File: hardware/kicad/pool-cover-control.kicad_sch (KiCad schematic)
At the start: 70 parts, among them J1 Power_Supply _Conn, J2 Motor_Conn, J3 Key_Switch_Conn, J4 Limit_Switch_Conn, J5 SWD_Conn, Q1 DMP4015SK3Q-13, U1 STM32G031K8Tx, U2 ULN2003A, U3 LMR14206, U4 PC817, U5 PC817, U6 PC817, U7 PC817

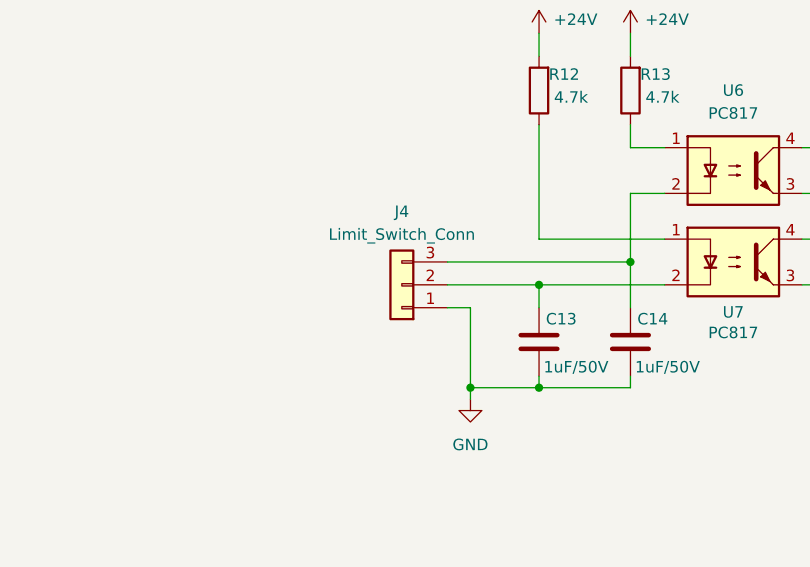
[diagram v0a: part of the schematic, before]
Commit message: feat(hardware): add 24 vcc pin to limit switch conn for flexibility
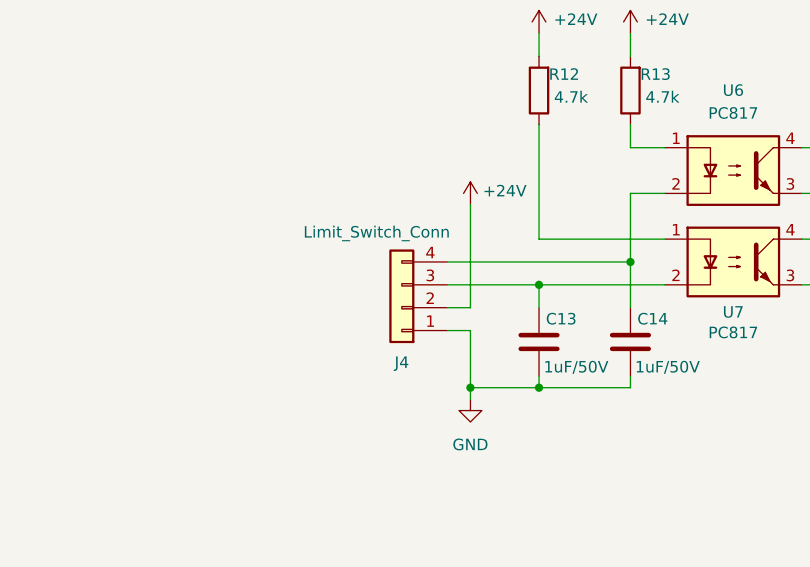
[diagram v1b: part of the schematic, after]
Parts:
- removed J4: Limit_Switch_Conn, TerminalBlock_Phoenix:TerminalBlock_Phoenix_MKDS-1,5-3-5.08_1x03_P5.08mm_Horizontal, symbol Connector_Generic:Conn_01x03
- added J4: Limit_Switch_Conn, TerminalBlock_Phoenix:TerminalBlock_Phoenix_MKDS-1,5-4-5.08_1x04_P5.08mm_Horizontal, symbol Connector_Generic:Conn_01x04
- C13, C14, C15, C16: footprint Capacitor_SMD:C_0402_1005Metric -> Capacitor_SMD:C_0603_1608Metric
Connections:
- net +24V: now also J4.2 (Pin_2)
- net GND: now also J4.1 (Pin_1)
- net at C14.2, U6.2: now also J4.4 (Pin_4)
- net at C13.2, U7.2: now also J4.3 (Pin_3)
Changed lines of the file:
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@@
 	)
 	(junction
-		(at 251.46 143.51)
-		(diameter 0)
-		(color 0 0 0 0)
-	)
-	(junction
 		(at 102.87 134.62)
 		(diameter 0)
@@
 	)
 	(junction
+		(at 251.46 143.51)
+		(diameter 0)
+		(color 0 0 0 0)
+	)
+	(junction
 		(at 259.08 132.08)
 		(diameter 0)
@@
 	(wire
 		(pts
+			(xy 251.46 137.16) (xy 251.46 143.51)
+		)
+		(stroke
+			(width 0)
+			(type default)
+		)
+	)
+	(wire
+		(pts
 			(xy 113.03 114.3) (xy 106.68 114.3)
 		)
@@
 	(wire
 		(pts
+			(xy 248.92 137.16) (xy 251.46 137.16)
+		)
+		(stroke
+			(width 0)
+			(type default)
+		)
+	)
+	(wire
+		(pts
 			(xy 125.73 189.23) (xy 142.24 189.23)
 		)
@@
 	(wire
 		(pts
-			(xy 251.46 134.62) (xy 248.92 134.62)
-		)
-		(stroke
-			(width 0)
-			(type default)
-		)
-	)
-	(wire
-		(pts
 			(xy 175.26 134.62) (xy 181.61 134.62)
 		)
@@
 	(wire
 		(pts
-			(xy 251.46 134.62) (xy 251.46 143.51)
-		)
-		(stroke
-			(width 0)
-			(type default)
-		)
-	)
-	(wire
-		(pts
 			(xy 248.92 132.08) (xy 259.08 132.08)
 		)
@@
 		)
 	)
+	(wire
+		(pts
+			(xy 248.92 134.62) (xy 251.46 134.62)
+		)
+		(stroke
+			(width 0)
+			(type default)
+		)
+	)
+	(wire
+		(pts
+			(xy 251.46 134.62) (xy 251.46 123.19)
+		)
+		(stroke
+			(width 0)
+			(type default)
+		)
+	)
 	(text "Reverse Polarity Protection\nP-channel MOSFET in series with the supply rail, gate clamped to −18V by a Zener diode,\nthat blocks current silently if the PSU is connected with reversed polarity."
 		(exclude_from_sim no)
@@
 			)
 		)
-		(property "Footprint" "Capacitor_SMD:C_0402_1005Metric"
+		(property "Footprint" "Capacitor_SMD:C_0603_1608Metric"
 			(at 258.1148 134.62 0)
 			(effects
@@
 			)
 		)
-		(property "Footprint" "Capacitor_SMD:C_0402_1005Metric"
+		(property "Footprint" "Capacitor_SMD:C_0603_1608Metric"
 			(at 268.2748 134.62 0)
 			(effects
@@
 			)
 		)
-		(property "Footprint" "Capacitor_SMD:C_0402_1005Metric"
+		(property "Footprint" "Capacitor_SMD:C_0603_1608Metric"
 			(at 258.1148 76.2 0)
 			(effects
@@
 	)
 	(symbol
+		(lib_id "power:+24V")
+		(at 251.46 123.19 0)
+		(unit 1)
+		(exclude_from_sim no)
+		(in_bom yes)
+		(on_board yes)
+		(dnp no)
+		(property "Reference" "#PWR1"
+			(at 251.46 127 0)
+			(effects
+				(font
+					(size 1.27 1.27)
+				)
+				(hide yes)
+			)
+		)
+		(property "Value" "+24V"
+			(at 255.27 121.666 0)
+			(effects
+				(font
+					(size 1.27 1.27)
+				)
+			)
+		)
+		(property "Footprint" ""
+			(at 251.46 123.19 0)
+			(effects
+				(font
+					(size 1.27 1.27)
+				)
+				(hide yes)
+			)
+		)
+		(property "Datasheet" ""
+			(at 251.46 123.19 0)
+			(effects
+				(font
+					(size 1.27 1.27)
+				)
+				(hide yes)
+			)
+		)
+		(property "Description" "Power symbol creates a global label with name \"+24V\""
+			(at 251.46 123.19 0)
+			(effects
+				(font
+					(size 1.27 1.27)
+				)
+				(hide yes)
+			)
+		)
+		(pin "1"
+		)
+		(instances
+			(project "pool-cover-control"
+				(path "/5c20c9eb-2c9b-4810-9f42-05cc49ca5670"
+					(reference "#PWR1")
+					(unit 1)
+				)
+			)
+		)
+	)
+	(symbol
 		(lib_id "Device:C")
 		(at 163.83 189.23 270)
@@
 	)
 	(symbol
-		(lib_id "Connector_Generic:Conn_01x03")
-		(at 243.84 132.08 180)
-		(unit 1)
-		(exclude_from_sim no)
-		(in_bom yes)
-		(on_board yes)
-		(dnp no)
-		(property "Reference" "J4"
-			(at 243.84 123.952 0)
-			(effects
-				(font
-					(size 1.27 1.27)
-				)
-			)
-		)
-		(property "Value" "Limit_Switch_Conn"
-			(at 243.84 126.492 0)
-			(effects
-				(font
-					(size 1.27 1.27)
-				)
-			)
-		)
-		(property "Footprint" "TerminalBlock_Phoenix:TerminalBlock_Phoenix_MKDS-1,5-3-5.08_1x03_P5.08mm_Horizontal"
-			(at 243.84 132.08 0)
-			(effects
-				(font
-					(size 1.27 1.27)
-				)
-				(hide yes)
-			)
-		)
-		(property "Datasheet" "~"
-			(at 243.84 132.08 0)
-			(effects
-				(font
-					(size 1.27 1.27)
-				)
-				(hide yes)
-			)
-		)
-		(property "Description" "Generic connector, single row, 01x03, script generated (kicad-library-utils/schlib/autogen/connector/)"
-			(at 243.84 132.08 0)
-			(effects
-				(font
-					(size 1.27 1.27)
-				)
-				(hide yes)
-			)
-		)
-		(property "LCSC" "C91154"
-			(at 243.84 132.08 0)
-			(effects
-				(font
-					(size 1.27 1.27)
-				)
-				(hide yes)
-			)
-		)
-		(pin "1"
-		)
-		(pin "2"
-		)
-		(pin "3"
-		)
-		(instances
-			(project "pool-cover-control"
-				(path "/5c20c9eb-2c9b-4810-9f42-05cc49ca5670"
-					(reference "J4")
-					(unit 1)
-				)
-			)
-		)
-	)
-	(symbol
 		(lib_id "Device:R")
 		(at 171.45 189.23 270)
@@
 			)
 		)
-		(property "Footprint" "Capacitor_SMD:C_0402_1005Metric"
+		(property "Footprint" "Capacitor_SMD:C_0603_1608Metric"
 			(at 268.2748 76.2 0)
 			(effects
@@
 					(unit 1)
 				)
+			)
+		)
+	)
+	(symbol
+		(lib_id "Connector_Generic:Conn_01x04")
+		(at 243.84 134.62 180)
+		(unit 1)
+		(exclude_from_sim no)
+		(in_bom yes)
+		(on_board yes)
+		(dnp no)
+		(property "Reference" "J4"
+			(at 243.84 140.716 0)
+			(effects
+				(font
+					(size 1.27 1.27)
+				)
+			)
+		)
+		(property "Value" "Limit_Switch_Conn"
+			(at 241.046 126.238 0)
+			(effects
+				(font
+					(size 1.27 1.27)
+				)
+			)
+		)
+		(property "Footprint" "TerminalBlock_Phoenix:TerminalBlock_Phoenix_MKDS-1,5-4-5.08_1x04_P5.08mm_Horizontal"
+			(at 243.84 134.62 0)
+			(effects
+				(font
+					(size 1.27 1.27)
+				)
+				(hide yes)
+			)
+		)
+		(property "Datasheet" "docs/datasheets/PhoenixContact1712805.pdf"
+			(at 243.84 134.62 0)
+			(effects
+				(font
+					(size 1.27 1.27)
+				)
+				(hide yes)
+			)
+		)
+		(property "Description" "Generic connector, single row, 01x04, script generated (kicad-library-utils/schlib/autogen/connector/)"
+			(at 243.84 134.62 0)
+			(effects
+				(font
+					(size 1.27 1.27)
+				)
+				(hide yes)
+			)
+		)
+		(property "LCSC" "C90087"
+			(at 243.84 134.62 0)
+			(effects
+				(font
+					(size 1.27 1.27)
+				)
+				(hide yes)
+			)
+		)
+		(pin "2"
+		)
+		(pin "4"
+		)
+		(pin "3"
+		)
+		(pin "1"
+		)
+		(instances
+			(project "pool-cover-control"
+				(path "/5c20c9eb-2c9b-4810-9f42-05cc49ca5670"
+					(reference "J4")
+					(unit 1)
+				)

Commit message: feat(hardware): update resistors out of stock in lcsc
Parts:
- C11, C12, C17, C18, C20, C5: value 100nF/10V -> 100nF/100V
- C7: value 4.7uF/10V -> 4.7uF/50V
- R10, R11, R14, R15: LCSC C48392572 -> C2906941
- R18: LCSC C144808 -> C2906860
- R4, R5, R6, R7: LCSC C177347 -> C2906981
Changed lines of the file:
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@@
 			)
 		)
-		(property "LCSC" "C48392572"
+		(property "LCSC" "C2906941"
 			(at 302.26 52.07 0)
 			(effects
@@
 			)
 		)
-		(property "LCSC" "C48392572"
+		(property "LCSC" "C2906941"
 			(at 292.1 52.07 0)
 			(effects
@@
 			)
 		)
-		(property "LCSC" "C177347"
+		(property "LCSC" "C2906981"
 			(at 111.76 146.05 90)
 			(effects
@@
 			)
 		)
-		(property "LCSC" "C177347"
+		(property "LCSC" "C2906981"
 			(at 173.99 146.05 90)
 			(effects
@@
 			)
 		)
-		(property "Value" "100nF/10V"
+		(property "Value" "100nF/100V"
 			(at 302.768 136.144 0)
 			(effects
@@
 			)
 		)
-		(property "Value" "100nF/10V"
+		(property "Value" "100nF/100V"
 			(at 302.768 77.724 0)
 			(effects
@@
 			)
 		)
-		(property "LCSC" "C177347"
+		(property "LCSC" "C2906981"
 			(at 113.03 189.23 90)
 			(effects
@@
 			)
 		)
-		(property "Value" "100nF/10V"
+		(property "Value" "100nF/100V"
 			(at 390.652 193.802 0)
 			(effects
@@
 			)
 		)
-		(property "Value" "100nF/10V"
+		(property "Value" "100nF/100V"
 			(at 258.064 187.198 0)
 			(effects
@@
 			)
 		)
-		(property "Value" "100nF/10V"
+		(property "Value" "100nF/100V"
 			(at 316.992 135.89 0)
 			(effects
@@
 			)
 		)
-		(property "LCSC" "C48392572"
+		(property "LCSC" "C2906941"
 			(at 292.1 110.49 0)
 			(effects
@@
 			)
 		)
-		(property "LCSC" "C177347"
+		(property "LCSC" "C2906981"
 			(at 171.45 189.23 90)
 			(effects
@@
 			)
 		)
-		(property "Value" "4.7uF/10V"
+		(property "Value" "4.7uF/50V"
 			(at 371.348 193.802 0)
 			(effects
@@
 			)
 		)
-		(property "LCSC" "C48392572"
+		(property "LCSC" "C2906941"
 			(at 302.26 110.49 0)
 			(effects
@@
 			)
 		)
-		(property "Value" "100nF/10V"
+		(property "Value" "100nF/100V"
 			(at 316.992 77.47 0)
 			(effects
@@
 			)
 		)
-		(property "LCSC" "C144808"
+		(property "LCSC" "C2906860"
 			(at 58.42 241.3 0)
 			(effects

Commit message: feat(hardware): add useful testpoints in layout
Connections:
- net LMR14206_SW: now reaches C3.2, D1.1 (K), L1.1, U3.6 (SW)
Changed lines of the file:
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@@
+		)
+	)
+	(label "LMR14206_SW"
+		(at 157.48 54.61 0)
+		(effects
+			(font
+				(size 1.27 1.27)
+			)
+			(justify left bottom)
 		)
 	)

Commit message: feat(hardware): add custom footprint for fuse holder and optos
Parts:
- F1: footprint Fuse:Fuseholder_Blade_Mini_Keystone_3568 -> pool-cover-control:Fuseholder_Blade_Mini_XFCN XF-508P-A-B
- J3: LCSC C91154 -> C91156
- U4, U5, U6, U7: footprint Package_SO:SOP-4_4.4x2.6mm_P1.27mm -> pool-cover-control:SOP-4_7.5x4.1mm_P2.54mm
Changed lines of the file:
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@@
 			)
 		)
-		(property "Footprint" "Package_SO:SOP-4_4.4x2.6mm_P1.27mm"
+		(property "Footprint" "pool-cover-control:SOP-4_7.5x4.1mm_P2.54mm"
 			(at 275.59 124.46 0)
 			(effects
@@
 			)
 		)
-		(property "Footprint" "Package_SO:SOP-4_4.4x2.6mm_P1.27mm"
+		(property "Footprint" "pool-cover-control:SOP-4_7.5x4.1mm_P2.54mm"
 			(at 275.59 76.2 0)
 			(effects
@@
 			)
 		)
-		(property "LCSC" "C91154"
+		(property "LCSC" "C91156"
 			(at 243.84 73.66 0)
 			(effects
@@
 			)
 		)
-		(property "Footprint" "Fuse:Fuseholder_Blade_Mini_Keystone_3568"
+		(property "Footprint" "pool-cover-control:Fuseholder_Blade_Mini_XFCN XF-508P-A-B"
 			(at 82.55 57.658 90)
 			(effects
@@
 			)
 		)
-		(property "Footprint" "Package_SO:SOP-4_4.4x2.6mm_P1.27mm"
+		(property "Footprint" "pool-cover-control:SOP-4_7.5x4.1mm_P2.54mm"
 			(at 275.59 66.04 0)
 			(effects
@@
 			)
 		)
-		(property "Footprint" "Package_SO:SOP-4_4.4x2.6mm_P1.27mm"
+		(property "Footprint" "pool-cover-control:SOP-4_7.5x4.1mm_P2.54mm"
 			(at 275.59 134.62 0)
 			(effects

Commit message: fix(hardware): review for JLCPCB standard parts
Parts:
- C10, C6, C8, C9: value 10nF/100V -> 10nF/50V; LCSC C43253 -> C57112
- C11, C12, C17, C18, C20, C5: value 100nF/100V -> 100nF/16V; LCSC C162178 -> C1525
- C13, C14, C15, C16: LCSC C92848 -> C15849
- C2: footprint Capacitor_SMD:C_0805_2012Metric -> Capacitor_SMD:C_1206_3216Metric; LCSC C2762602 -> 1206
- C3: value 0.15uF -> 220nF; LCSC C513735 -> C21120
- C4: value 47uF/10V -> 22uF/25V; footprint Capacitor_SMD:C_0805_2012Metric -> Capacitor_SMD:C_1206_3216Metric; LCSC C19103846 -> C12891
- C7: value 4.7uF/50V -> 4.7uF/25V; LCSC C7472970 -> C1779
- LED1: LCSC C19273151 -> C2286
- LED2: LCSC C19171394 -> C2286
- LED3: LCSC C19273152 -> C2286
- LED4: LCSC C19171390 -> C2286
- R1: LCSC C2906859 -> C25741
- R10, R11, R14, R15: LCSC C2906941 -> C25900
- R12, R13, R8, R9: LCSC C54532891 -> C17936
- R16: footprint Resistor_SMD:R_0402_1005Metric -> Resistor_SMD:R_0603_1608Metric; LCSC C60490 -> C25804
- R17, R19, R20: LCSC C2906929 -> C25104
- R18: value 100 -> 330; LCSC C2906860 -> C25104
- R2: value 1.02k -> 3k; footprint Resistor_SMD:R_0402_1005Metric -> Resistor_SMD:R_0603_1608Metric; LCSC C852594 -> C4211
- R3: value 3.4k -> 10k; footprint Resistor_SMD:R_0402_1005Metric -> Resistor_SMD:R_0603_1608Metric; LCSC C852765 -> C25804
- R4, R5, R6, R7: LCSC C2906981 -> C22775
- U2: LCSC C253892 -> C7512
